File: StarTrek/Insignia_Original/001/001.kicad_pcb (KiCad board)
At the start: 2 copper layers, 58 x 93.5 mm, 6 parts, among them U1 StarTrek_Original, U2 Firma, U3 PinBase

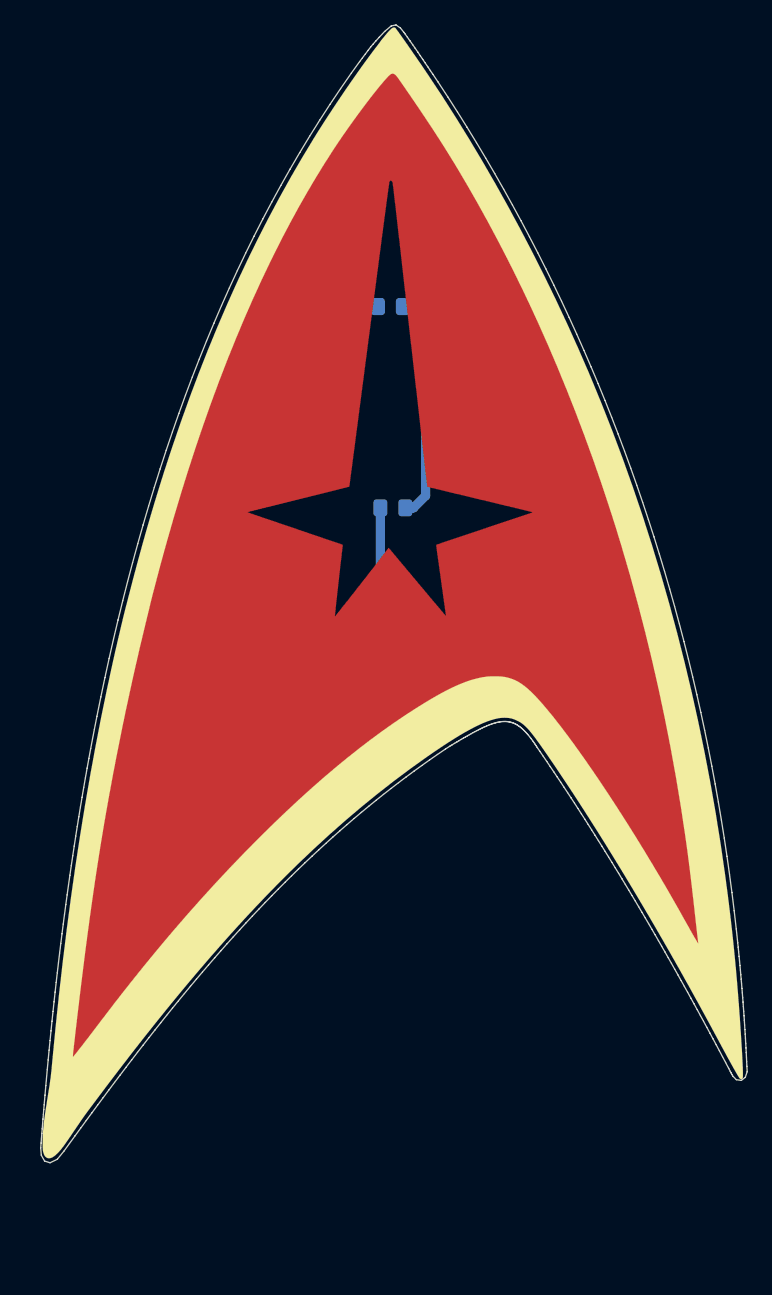
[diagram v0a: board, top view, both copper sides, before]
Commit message: Add Moon Reverse Led Kit
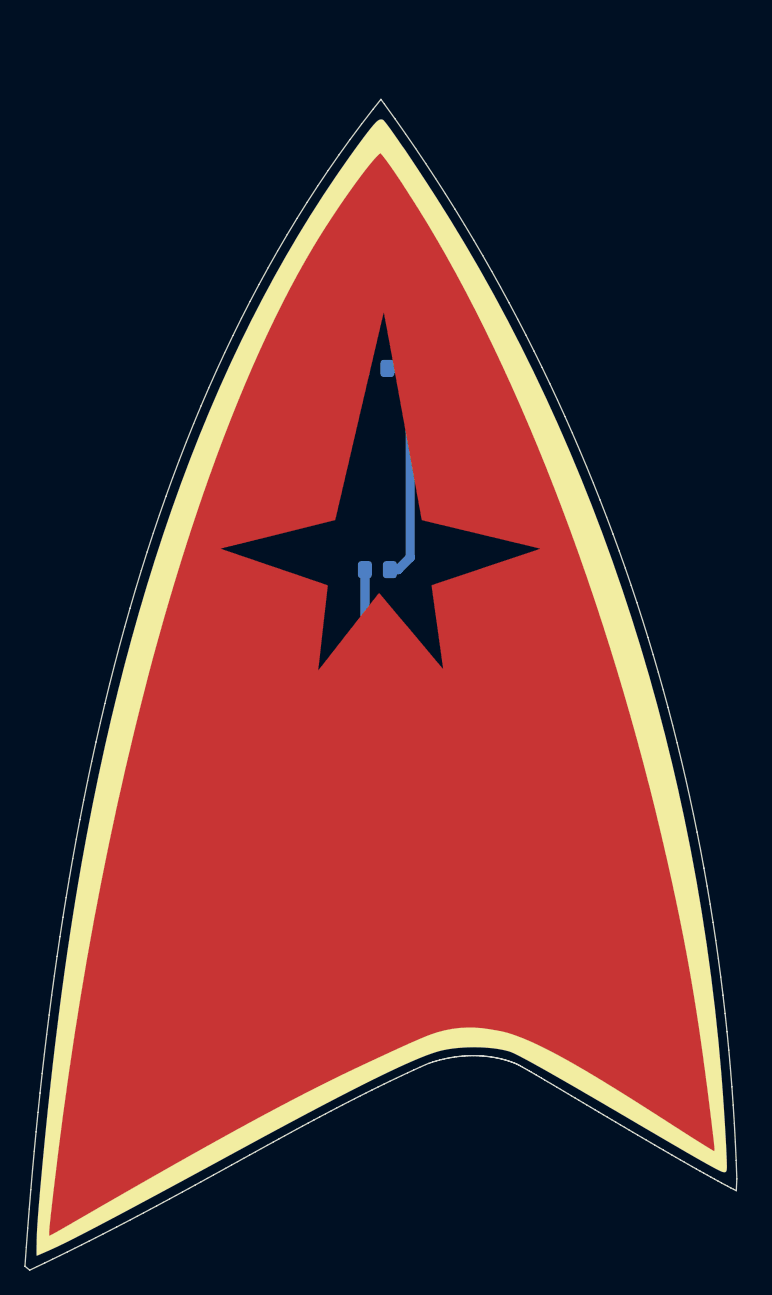
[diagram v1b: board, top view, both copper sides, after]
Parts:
- removed U1: StarTrek_Original, StarTrek_original:Star_Trek_Original_Series_Insignia_100mm
- added Ref**: Val**, StarTrek_original:TOS_Insignia_100mm_001, F.Cu at (139.1, 92.7)
- moved U2 5.24 mm to (153.9, 98.9)
- moved U3 5.24 mm to (136.8, 53.6)
- moved D1 5.24 mm to (136.7, 67.2)
- moved D2 5.24 mm to (136.9, 83.7)
- moved BT1 5.24 mm to (123.3, 103.6)
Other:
- board size 58 x 93.5 mm -> 58.5 x 96.2 mm
